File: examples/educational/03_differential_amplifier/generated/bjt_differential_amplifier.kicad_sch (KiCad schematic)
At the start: 8 parts, among them Q1 BC547, Q2 BC547

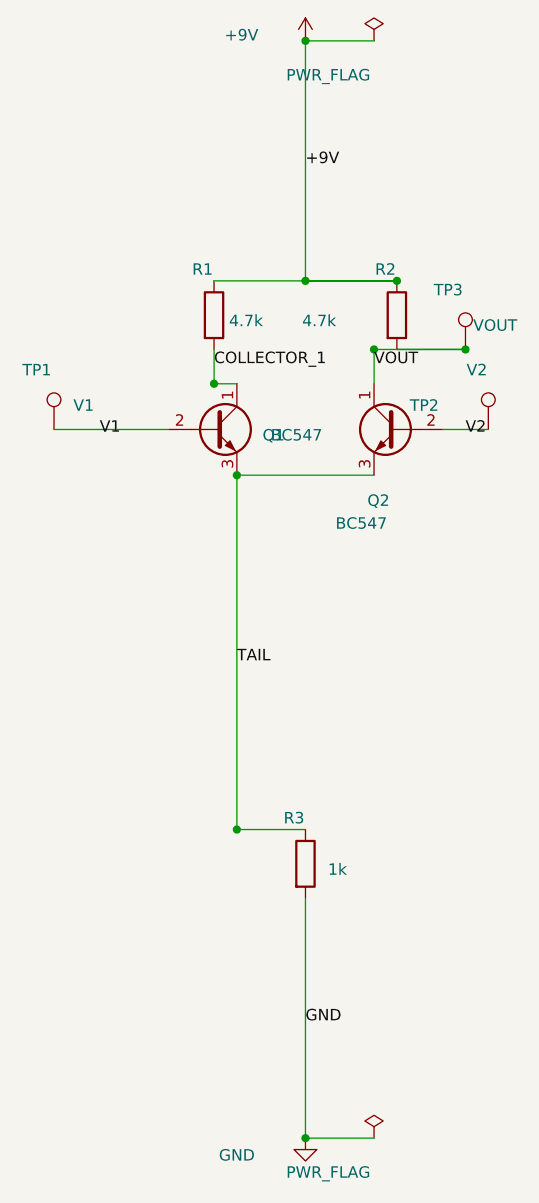
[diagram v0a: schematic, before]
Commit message: feat: infer conventional schematic topology layouts
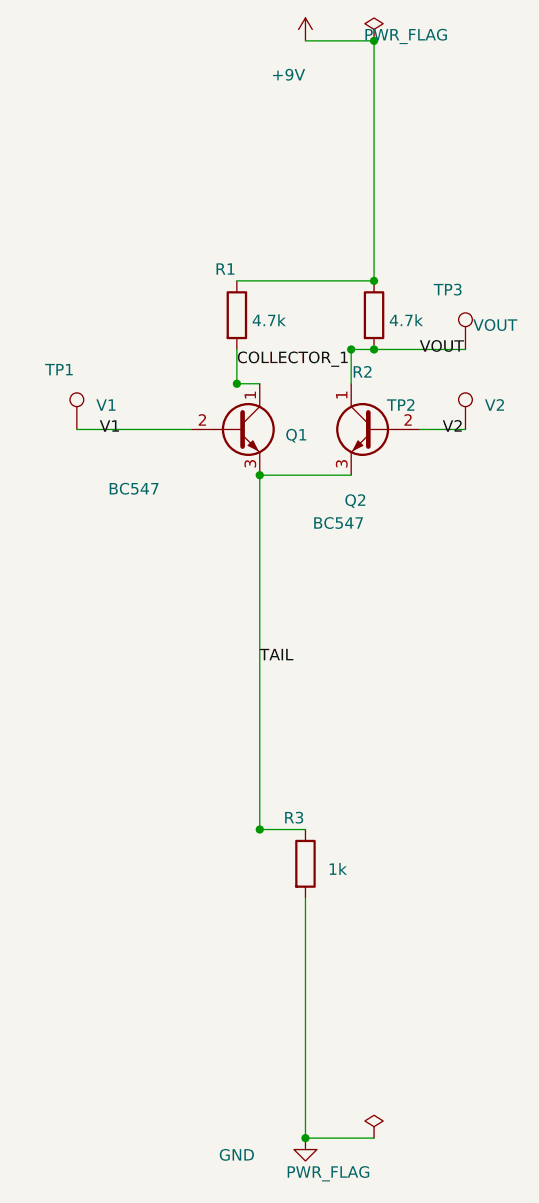
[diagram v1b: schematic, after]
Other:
- moved on the sheet: Q1, Q2, R1, R2, TP1, TP2
